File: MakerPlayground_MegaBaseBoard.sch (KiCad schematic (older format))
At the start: 61 parts, among them J1 BattCon, J10 D5, J11 D6, J12 I2C, J13 I2C, J14 D1/A4, J15 D2/A5, J16 I2C, J2 ESP32, J3 USB, J4 Micro_SD_Card, J5 A1, J6 A2, J7 A3, J8 D3, J9 D4, Q1 Q_NPN_BEC, Q2 Q_NPN_BEC, SW1 Reset, U1 MCP73871, U2 TPS63001, U3 CP2102N-A01-GQFN24, U4 TXB0108DQSR

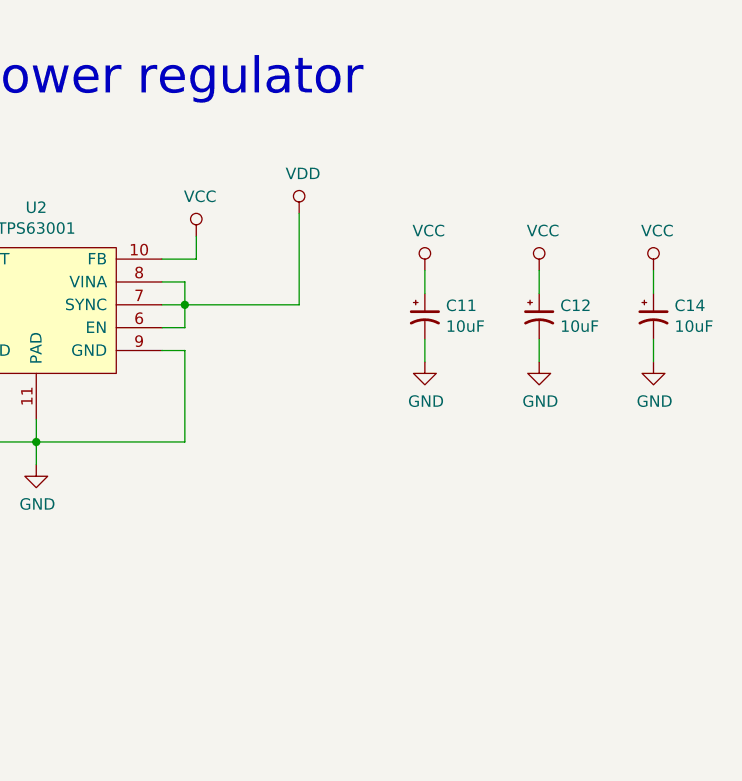
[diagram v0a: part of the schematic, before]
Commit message: Add ON/OFF switch & new alignment for PWR/CHG LED.
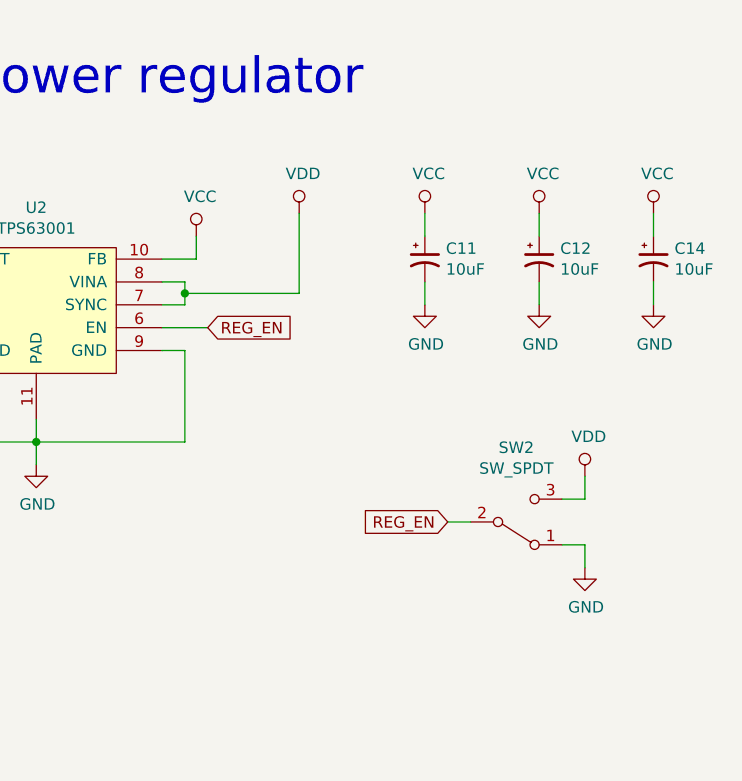
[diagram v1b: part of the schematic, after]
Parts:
- added SW2: SW_SPDT, GiraffeTech-Electromechanical:SW_SPDT_CK-JS102011JCQN, symbol Switch:SW_SPDT
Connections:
- net GND: now also SW2.1 (A)
- net VDD: now also SW2.3 (C); no longer U2.6 (EN)
- new net REG_EN: SW2.2 (B), U2.6 (EN)
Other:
- moved on the sheet: C11, C12, C14
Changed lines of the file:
@@
 EESchema Schematic File Version 4
-LIBS:MakerPlayground_ESP32BaseBoard_v1.0-cache
 EELAYER 26 0
 EELAYER END
@@
 	13100 5300 13200 5300
 Wire Wire Line
-	13200 5300 13200 5400
+	13200 5300 13200 5350
 Wire Wire Line
 	13100 5400 13200 5400
-Connection ~ 13200 5400
-Wire Wire Line
-	13200 5400 13700 5400
 $Comp
 L power:VDD #PWR0121
@@
 L Device:CP1_Small C11
 U 1 1 5BCF9152
-P 14250 5450
-F 0 "C11" H 14342 5496 50  0000 L CNN
-F 1 "10uF" H 14342 5405 50  0000 L CNN
-F 2 "Capacitor_SMD:C_0805_2012Metric" H 14250 5450 50  0001 C CNN
-F 3 "~" H 14250 5450 50  0001 C CNN
-	1    14250 5450
-	1    0    0    -1
-$EndComp
-Wire Wire Line
-	14250 5250 14250 5350
+P 14250 5200
+F 0 "C11" H 14342 5246 50  0000 L CNN
+F 1 "10uF" H 14342 5155 50  0000 L CNN
+F 2 "Capacitor_SMD:C_0805_2012Metric" H 14250 5200 50  0001 C CNN
+F 3 "~" H 14250 5200 50  0001 C CNN
+	1    14250 5200
+	1    0    0    -1
+$EndComp
+Wire Wire Line
+	14250 5000 14250 5100
 $Comp
 L power:GND #PWR0123
 U 1 1 5BCFD185
-P 14250 5650
-F 0 "#PWR0123" H 14250 5400 50  0001 C CNN
-F 1 "GND" H 14255 5477 50  0000 C CNN
-F 2 "" H 14250 5650 50  0001 C CNN
-F 3 "" H 14250 5650 50  0001 C CNN
-	1    14250 5650
-	1    0    0    -1
-$EndComp
-Wire Wire Line
-	14250 5550 14250 5650
+P 14250 5400
+F 0 "#PWR0123" H 14250 5150 50  0001 C CNN
+F 1 "GND" H 14255 5227 50  0000 C CNN
+F 2 "" H 14250 5400 50  0001 C CNN
+F 3 "" H 14250 5400 50  0001 C CNN
+	1    14250 5400
+	1    0    0    -1
+$EndComp
+Wire Wire Line
+	14250 5300 14250 5400
 $Comp
 L Device:CP1_Small C12
 U 1 1 5BD01250
-P 14750 5450
-F 0 "C12" H 14842 5496 50  0000 L CNN
-F 1 "10uF" H 14842 5405 50  0000 L CNN
-F 2 "Capacitor_SMD:C_0805_2012Metric" H 14750 5450 50  0001 C CNN
-F 3 "~" H 14750 5450 50  0001 C CNN
-	1    14750 5450
-	1    0    0    -1
-$EndComp
-Wire Wire Line
-	14750 5250 14750 5350
+P 14750 5200
+F 0 "C12" H 14842 5246 50  0000 L CNN
+F 1 "10uF" H 14842 5155 50  0000 L CNN
+F 2 "Capacitor_SMD:C_0805_2012Metric" H 14750 5200 50  0001 C CNN
+F 3 "~" H 14750 5200 50  0001 C CNN
+	1    14750 5200
+	1    0    0    -1
+$EndComp
+Wire Wire Line
+	14750 5000 14750 5100
 $Comp
 L power:GND #PWR0124
 U 1 1 5BD01257
-P 14750 5650
-F 0 "#PWR0124" H 14750 5400 50  0001 C CNN
-F 1 "GND" H 14755 5477 50  0000 C CNN
-F 2 "" H 14750 5650 50  0001 C CNN
-F 3 "" H 14750 5650 50  0001 C CNN
-	1    14750 5650
-	1    0    0    -1
-$EndComp
-Wire Wire Line
-	14750 5550 14750 5650
+P 14750 5400
+F 0 "#PWR0124" H 14750 5150 50  0001 C CNN
+F 1 "GND" H 14755 5227 50  0000 C CNN
+F 2 "" H 14750 5400 50  0001 C CNN
+F 3 "" H 14750 5400 50  0001 C CNN
+	1    14750 5400
+	1    0    0    -1
+$EndComp
+Wire Wire Line
+	14750 5300 14750 5400
 $Comp
 L power:VBUS #PWR0125
@@
 L power:VCC #PWR0142
 U 1 1 5BF25736
-P 14250 5250
-F 0 "#PWR0142" H 14250 5100 50  0001 C CNN
-F 1 "VCC" H 14267 5423 50  0000 C CNN
-F 2 "" H 14250 5250 50  0001 C CNN
-F 3 "" H 14250 5250 50  0001 C CNN
-	1    14250 5250
+P 14250 5000
+F 0 "#PWR0142" H 14250 4850 50  0001 C CNN
+F 1 "VCC" H 14267 5173 50  0000 C CNN
+F 2 "" H 14250 5000 50  0001 C CNN
+F 3 "" H 14250 5000 50  0001 C CNN
+	1    14250 5000
 	1    0    0    -1
 $EndComp
@@
 L power:VCC #PWR0143
 U 1 1 5BF25797
-P 14750 5250
-F 0 "#PWR0143" H 14750 5100 50  0001 C CNN
-F 1 "VCC" H 14767 5423 50  0000 C CNN
-F 2 "" H 14750 5250 50  0001 C CNN
-F 3 "" H 14750 5250 50  0001 C CNN
-	1    14750 5250
+P 14750 5000
+F 0 "#PWR0143" H 14750 4850 50  0001 C CNN
+F 1 "VCC" H 14767 5173 50  0000 C CNN
+F 2 "" H 14750 5000 50  0001 C CNN
+F 3 "" H 14750 5000 50  0001 C CNN
+	1    14750 5000
 	1    0    0    -1
 $EndComp
@@
 D3_DAC2_1
 Wire Wire Line
-	13200 5500 13100 5500
-Wire Wire Line
-	13200 5400 13200 5500
-Wire Wire Line
 	1450 8200 2150 8200
 NoConn ~ 2150 7600
@@
 L Device:CP1_Small C14
 U 1 1 5BDE038D
-P 15250 5450
-F 0 "C14" H 15342 5496 50  0000 L CNN
-F 1 "10uF" H 15342 5405 50  0000 L CNN
-F 2 "Capacitor_SMD:C_0805_2012Metric" H 15250 5450 50  0001 C CNN
-F 3 "~" H 15250 5450 50  0001 C CNN
-	1    15250 5450
-	1    0    0    -1
-$EndComp
-Wire Wire Line
-	15250 5250 15250 5350
+P 15250 5200
+F 0 "C14" H 15342 5246 50  0000 L CNN
+F 1 "10uF" H 15342 5155 50  0000 L CNN
+F 2 "Capacitor_SMD:C_0805_2012Metric" H 15250 5200 50  0001 C CNN
+F 3 "~" H 15250 5200 50  0001 C CNN
+	1    15250 5200
+	1    0    0    -1
+$EndComp
+Wire Wire Line
+	15250 5000 15250 5100
 $Comp
 L power:GND #PWR0175
 U 1 1 5BDE0394
-P 15250 5650
-F 0 "#PWR0175" H 15250 5400 50  0001 C CNN
-F 1 "GND" H 15255 5477 50  0000 C CNN
-F 2 "" H 15250 5650 50  0001 C CNN
-F 3 "" H 15250 5650 50  0001 C CNN
-	1    15250 5650
-	1    0    0    -1
-$EndComp
-Wire Wire Line
-	15250 5550 15250 5650
+P 15250 5400
+F 0 "#PWR0175" H 15250 5150 50  0001 C CNN
+F 1 "GND" H 15255 5227 50  0000 C CNN
+F 2 "" H 15250 5400 50  0001 C CNN
+F 3 "" H 15250 5400 50  0001 C CNN
+	1    15250 5400
+	1    0    0    -1
+$EndComp
+Wire Wire Line
+	15250 5300 15250 5400
 $Comp
 L power:VCC #PWR0176
 U 1 1 5BDE039B
-P 15250 5250
-F 0 "#PWR0176" H 15250 5100 50  0001 C CNN
-F 1 "VCC" H 15267 5423 50  0000 C CNN
-F 2 "" H 15250 5250 50  0001 C CNN
-F 3 "" H 15250 5250 50  0001 C CNN
-	1    15250 5250
-	1    0    0    -1
-$EndComp
-Wire Wire Line
-	13700 5000 13700 5400
+P 15250 5000
+F 0 "#PWR0176" H 15250 4850 50  0001 C CNN
+F 1 "VCC" H 15267 5173 50  0000 C CNN
+F 2 "" H 15250 5000 50  0001 C CNN
+F 3 "" H 15250 5000 50  0001 C CNN
+	1    15250 5000
+	1    0    0    -1
+$EndComp
+Wire Wire Line
+	13700 5000 13700 5350
 $Comp
 L power:VBUS #PWR0177
@@
 Text GLabel 9300 10250 2    50   Input ~ 0
 IO_PWR
+Wire Wire Line
+	13200 5350 13700 5350
+Connection ~ 13200 5350
+Wire Wire Line
+	13200 5350 13200 5400
+$Comp
+L Switch:SW_SPDT SW2
+U 1 1 5BE8FE6D
+P 14650 6350
+F 0 "SW2" H 14650 6025 50  0000 C CNN
+F 1 "SW_SPDT" H 14650 6116 50  0000 C CNN
+F 2 "GiraffeTech-Electromechanical:SW_SPDT_CK-JS102011JCQN" H 14650 6350 50  0001 C CNN
+F 3 "" H 14650 6350 50  0001 C CNN
+	1    14650 6350
+	1    0    0    1
+$EndComp
+$Comp
+L power:GND #PWR0163
+U 1 1 5BE9075A
+P 14950 6550
+F 0 "#PWR0163" H 14950 6300 50  0001 C CNN
+F 1 "GND" H 14955 6377 50  0000 C CNN
+F 2 "" H 14950 6550 50  0001 C CNN
+F 3 "" H 14950 6550 50  0001 C CNN
+	1    14950 6550
+	1    0    0    -1
+$EndComp
+Wire Wire Line
+	14850 6450 14950 6450
+Wire Wire Line
+	14950 6450 14950 6550
+$Comp
+L power:VDD #PWR0165
+U 1 1 5BEA9C3D
+P 14950 6150
+F 0 "#PWR0165" H 14950 6000 50  0001 C CNN
+F 1 "VDD" H 14967 6323 50  0000 C CNN
+F 2 "" H 14950 6150 50  0001 C CNN
+F 3 "" H 14950 6150 50  0001 C CNN
+	1    14950 6150
+	1    0    0    -1
+$EndComp
+Wire Wire Line
+	14850 6250 14950 6250
+Wire Wire Line
+	14950 6250 14950 6150
+Text GLabel 13300 5500 2    50   Input ~ 0
+REG_EN
+Wire Wire Line
+	13100 5500 13300 5500
+Text GLabel 14350 6350 0    50   Input ~ 0
+REG_EN
+Wire Wire Line
+	14350 6350 14450 6350
 $EndSCHEMATC
